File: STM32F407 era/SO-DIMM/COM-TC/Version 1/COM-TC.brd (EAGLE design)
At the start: 127 x 165.1 mm, 126 parts, among them J1 CON1, J2 CON1, J3 SO-DIMM-CPU, J4 FTDI_DEVICE, Q4 PMV20XNE, U1 IRF9332PBF, U10 SN65HVD232D, U11 MAX9926, U12 MCP6004-E/SL, U13 MCP6004-E/SL, U14 MCP6004-E/SL, U17 MC74AC573DWG, U18 MC74AC573DWG, U19 MC74AC573DWG, U2 5V, U20 MC74AC573DWG, U3 TPS54331D, U4 3,3V, U5 MAX9926, U6 MCP6004-E/SL, U7 LoPy, X1 057-014-1

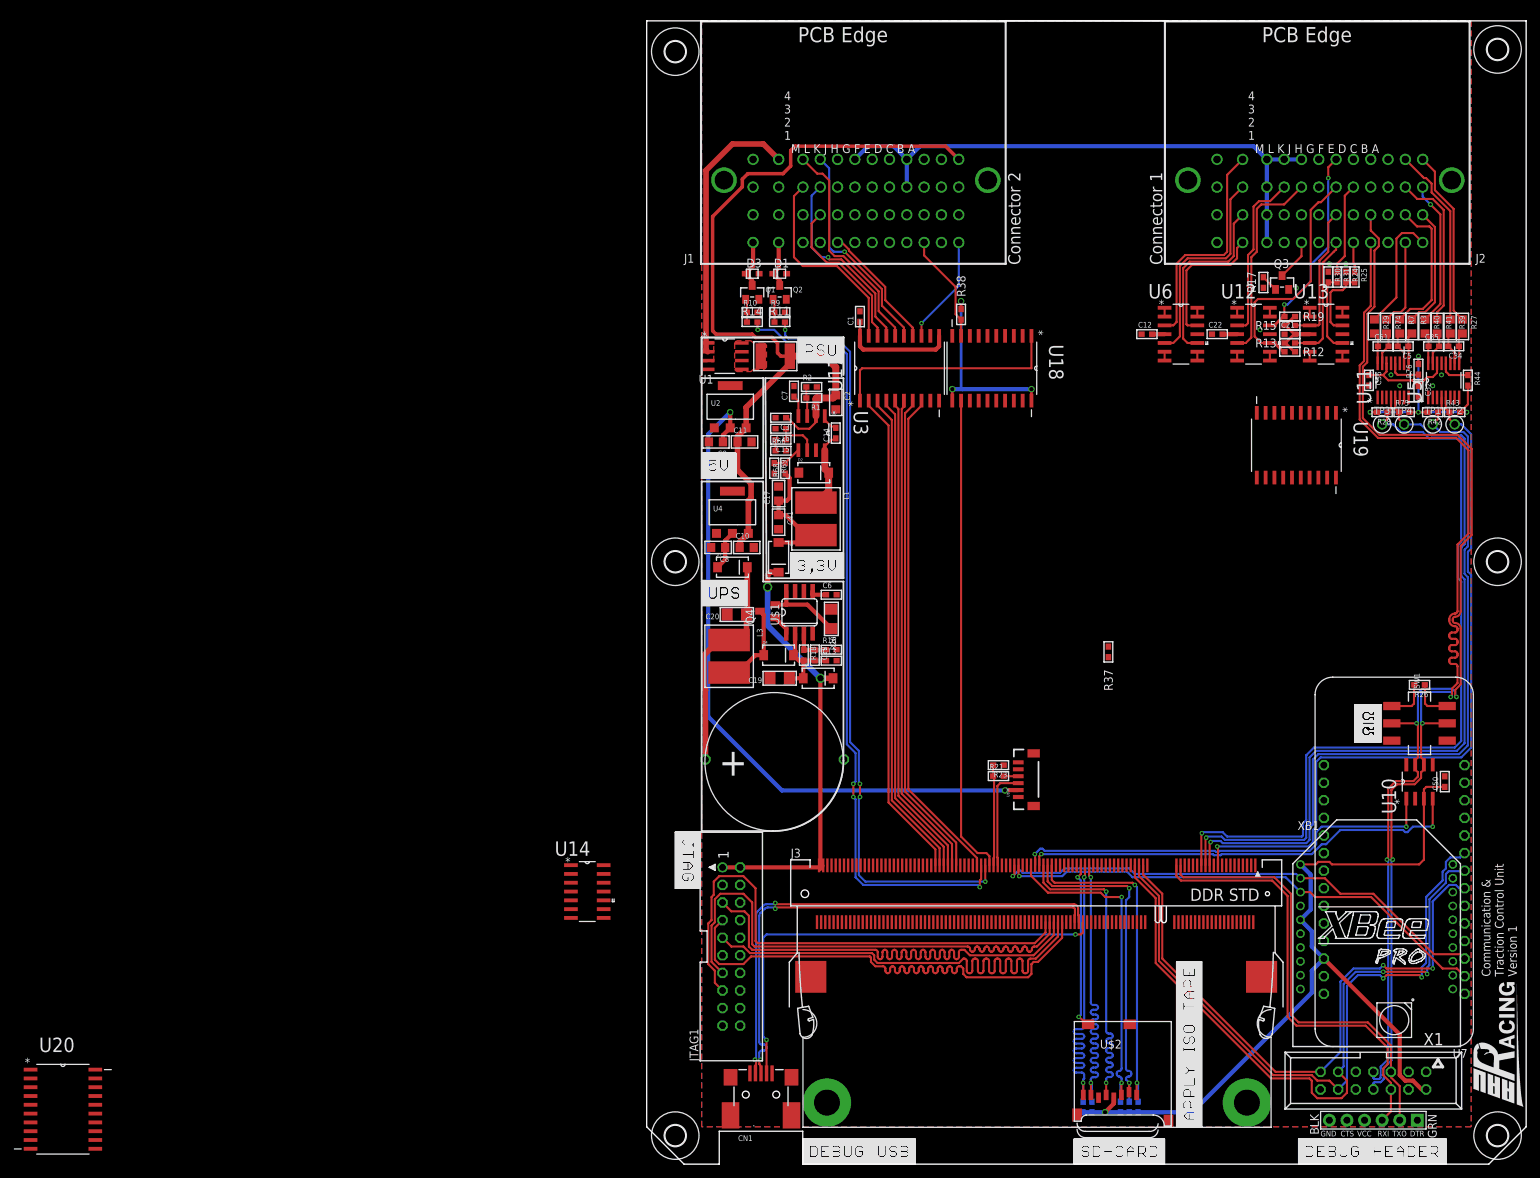
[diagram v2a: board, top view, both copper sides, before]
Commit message: COM/TC RC1 done
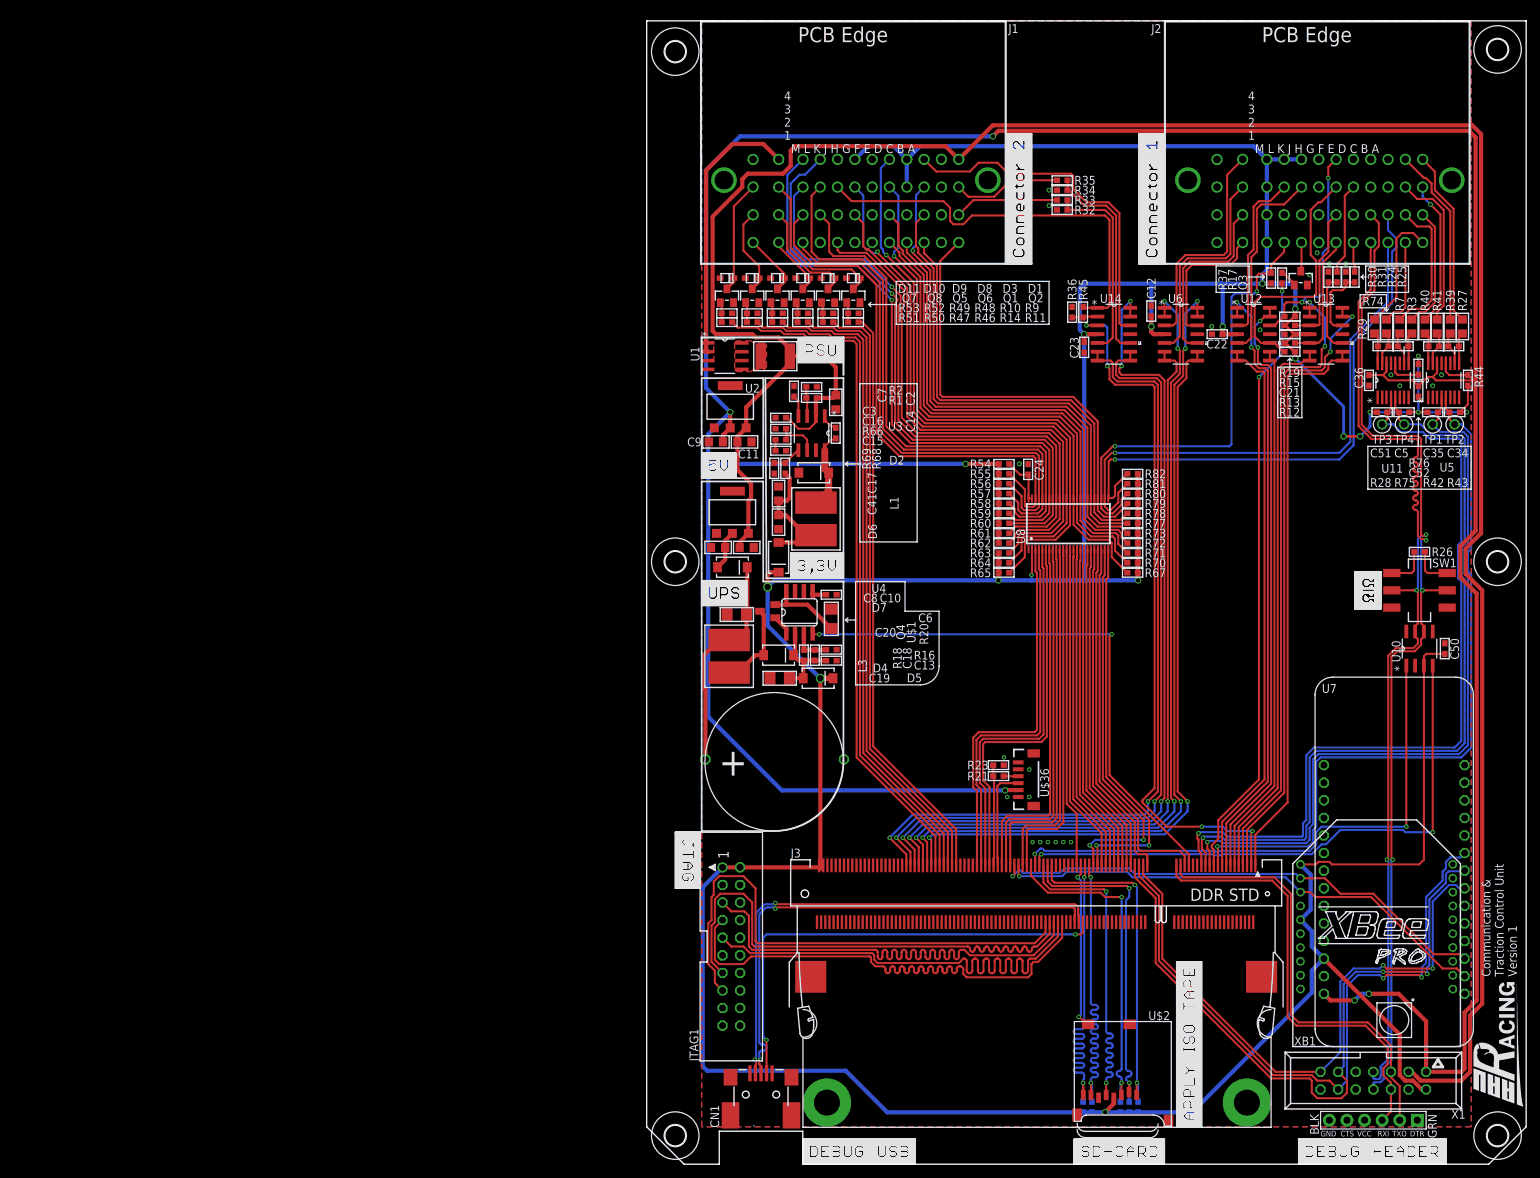
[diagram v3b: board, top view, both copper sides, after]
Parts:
- removed C1: 100n, microbuilder:_0603
- removed R38: 10k, microbuilder:_0603
- removed U17, U18, U19, U20: MC74AC573DWG, ON Semiconductor_By_element14_Batch_1:SOIC127P1030X265-20N
- added C23, C24: 100n, microbuilder:_0603
- added D10, D11, D8, D9: (no value), adafruit:SOD-323F
- added Q5, Q6, Q7, Q8: (no value), microbuilder:SOT23-WIDE
- added R32, R34, R36: 976, microbuilder:_0603
- added R33, R35, R45: 499, microbuilder:_0603
- added R46, R47, R50, R51, R55, R56, R57, R58, R59, R60, R61, R62, R63, R64, R65, R67, R70, R71, R72, R73, R77, R78, R79, R80, R81, R82: 220, microbuilder:_0603
- added R48, R49, R52, R53: 500, microbuilder:_0603
- added R54: 200k, microbuilder:_0603
- added U8: GTL2000, AAU-Racing:TSSOP48
- C10, C11: value (none) -> 10u
- C8, C9: value (none) -> 22u
- moved U14 110.7 mm to (67.5, 119.9)
- moved R37 58.9 mm to (90.2, 128.0)
- moved SW1 19.2 mm to (111.6, 82.9)
- moved C50 19.2 mm to (115.3, 74.5)
- moved U10 19.2 mm to (111.6, 74.5)
- moved R26 19.2 mm to (111.6, 88.4)
- moved D3 11.0 mm to (26.2, 128.0), turned to 0 degrees
- moved Q1 11.0 mm to (26.2, 125.4)
- moved R10 11.0 mm to (26.2, 122.9)
- moved R14 11.0 mm to (26.2, 121.6)
- moved D1 10.7 mm to (29.8, 128.0), turned to 0 degrees
- moved Q2 10.6 mm to (29.8, 125.4)
- moved R9 10.6 mm to (29.8, 122.9)
- moved R11 10.6 mm to (29.8, 121.6)
- moved C12 3.39 mm to (72.9, 123.2), turned to 270 degrees
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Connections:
- removed net BRAKE-POT: J1.C3
- removed net DIG_IO_EN: U17.1, U18.1
- removed net VOUTUB: J3.3
- new net AUX1: J1.G2, R63.2, U8.38
- new net AUX1L: J3.99, U8.11
- new net AUX2: J1.G3, R64.2, U8.37
- new net AUX2L: J3.75, U8.12
- new net AUX3: J1.E4, R65.2, U8.36
- new net AUX3L: J3.63, U8.13
- new net AUX4: J1.E3, R67.2, U8.35
- new net AUX4L: J3.61, U8.14
- new net AUX5: J1.E1, R70.2, U8.34
- new net AUX5L: J3.59, U8.15
- new net AUX6: J1.E2, R71.2, U8.33
- new net AUX6L: J3.57, U8.16
- new net AUX7: J1.D1, R72.2, U8.32
- new net AUX7L: J3.55, U8.17
- new net AUX8: J1.C3, R73.2, U8.31
- new net AUX8L: J3.53, U8.18
- new net AUX9: J1.C2, R77.2, U8.30
- new net AUX9L: J3.51, U8.19
- new net COM_RXB: J3.67, U8.23
- new net COM_TXB: J3.65, U8.24
- new net ECU1L: J3.123, U8.3
- new net ECU2L: J3.121, U8.4
- new net GSENSL: R32.2, R33.2, U14.5
- new net N$13: R36.2, R45.1, U14.2
- new net N$14: Q5.1, R47.1, R49.1
- new net N$20: Q8.1, R50.1, R52.1
- new net N$21: Q7.1, R51.1, R53.1
- new net N$23: C24.1, R54.1, U8.47, U8.48
- new net N$33: J1.H2
- new net N$9: Q6.1, R46.1, R48.1
- new net NEUTRALL: J3.35, U8.22
- new net ODC1: J3.135, R14.2
- new net ODC2: J3.141, R50.2
- new net ODC3: J3.133, R11.2
- new net ODC4: J3.143, R51.2
- new net ODI1: D3.C, J1.L2, Q1.3
- new net ODI2: D10.C, J1.M2, Q8.3
- new net ODI3: D1.C, J1.L3, Q2.3
- new net ODI4: D11.C, J1.M3, Q7.3
- new net VOUTB: J1.H3, R45.2, U14.1
- new net YAWL: R34.2, R35.2, U14.10
- net 3.3V: now also C23.2, R63.1, R64.1, R65.1, R67.1, R70.1, R71.1, R72.1, R73.1, R77.1, R78.1, R79.1, R80.1, R81.1, R82.1, U8.2; no longer R38.1, U18.11, U18.20
- net 5.0V: now also R54.2, R55.1, R56.1, R57.1, R58.1, R59.1, R60.1, R61.1, R62.1; no longer C1.1, U17.11, U17.20
- net BITE: now also R79.2, U8.28; no longer U17.13
- net BITEL: now also J3.41, U8.21; no longer J3.123, U17.8
- net BRAKEPB: now also J3.13; no longer J3.5
- net CLUTCH-POT: now also U14.12
- net CLUTCH-POTB: now also J3.153, U14.13, U14.14; no longer J3.145
- net COM_RX: now also R81.2, U8.26; no longer J3.67
- net COM_TX: now also R82.2, U8.25; no longer J3.65
- net CURRENT1B: now also J3.5; no longer J3.15
- net CURRENT2B: now also J3.1; no longer J3.17
- net ECU1: now also J1.K2, R55.2, U8.46; no longer J2.C4
- net ECU2: now also J1.K1, R56.2, U8.45; no longer J2.D4
- net GEARPOSANB: now also J3.17; no longer J3.9
- net GND: now also C23.1, C24.2, D10.A, D11.A, D8.A, D9.A, Q5.2, Q6.2, Q7.2, Q8.2, R32.1, R34.1, R36.1, R48.2, R49.2, R52.2, R53.2, U14.11, U8.1; no longer C1.2, U17.10, U17.9, U18.10
- net GSENS: now also R33.1
- net GSENSB: now also J3.157, U14.6, U14.7; no longer J3.155
- net HB1-DIRA: now also J3.101, U8.10; no longer J3.133, U17.7
- net HB1-DIRA-IN: now also R62.2, U8.39; no longer U17.14
- net HB1-DIRB: now also J3.109, U8.8; no longer J3.135, U17.6
- net HB1-DIRB-IN: now also R60.2, U8.41; no longer U17.15
- net HB1-PWM: now also J3.119, U8.5; no longer J3.139, U17.4
- net HB1-PWM-IN: now also R57.2, U8.44; no longer U17.17
- net HB2-DIRA: now also J3.107, U8.9; no longer J3.143, U17.2
- net HB2-DIRA-IN: now also R61.2, U8.40; no longer U17.19
- net HB2-DIRB: now also J3.111, U8.7; no longer J3.137, U17.5
- net HB2-DIRB-IN: now also R59.2, U8.42; no longer U17.16
- net HB2-PWM: now also J3.117, U8.6; no longer J3.141, U17.3
- net HB2-PWM-IN: now also R58.2, U8.43; no longer U17.18
- net IGNCUT: now also J3.21
- net NEUTRAL: now also R80.2, U8.27
- net OC1: now also J3.137, R46.2; no longer J3.119, R11.2
- net OC2: now also J3.139, R47.2; no longer J3.121, R14.2
- net OILP: now also R78.2, U8.29; no longer R38.2, U18.9
- net OILPI: now also J3.49, U8.20; no longer J3.117, U18.12
- net RLY1: now also D8.C, Q6.3; no longer D1.C, Q2.3
- net RLY2: now also D9.C, Q5.3; no longer D3.C, Q1.3
- net SPEEDB: now also J3.15; no longer J3.1
- net TRAVEL1B: now also J3.151; no longer J3.147
- net TRAVEL3B: now also J3.145; no longer J3.151
- net TRAVEL4B: now also J3.147; no longer J3.153
- net UPS_EN: now also J3.33
- net VCC: no longer U19.20, U20.20
- net VOUT: now also J3.3, U14.3; no longer J1.H3
- net VTEMP2B: now also J3.11; no longer J3.13
- net VTEMPB: now also J3.9; no longer J3.11
- net YAW: now also R35.1
- net YAWB: now also J3.155, U14.8, U14.9; no longer J3.157
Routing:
- net 5.0V: track 130.9 -> 491.4 mm, vias 2 -> 6
- net 3.3V: track 346.3 -> 628.9 mm, vias 10 -> 18
- net 12V: track 127.9 -> 353.7 mm
- net CLUTCH-POTB: track 0.00 -> 126.2 mm, vias 0 -> 4
- net TRAVEL2B: track 1.27 -> 120.8 mm, vias 0 -> 4
- net TRAVEL4B: track 1.27 -> 120.8 mm, vias 0 -> 4
- net GSENSB: track 0.00 -> 118.7 mm, vias 0 -> 2
- net YAWB: track 0.00 -> 118.2 mm, vias 0 -> 2
- net TRAVEL1B: track 1.27 -> 111.9 mm, vias 0 -> 2
- net TRAVEL3B: track 1.27 -> 111.9 mm, vias 0 -> 2
- net VOUT: track 0.00 -> 102.7 mm, vias 0 -> 4
- net ODC4: track 0.00 -> 99.3 mm
- net ODC2: track 0.00 -> 96.3 mm
- net BRAKEP2B: track 1.27 -> 92.1 mm, vias 0 -> 2
- net CURRENT1B: track 1.27 -> 91.1 mm, vias 0 -> 2
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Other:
- board text removed: "Connector 1"
- board text removed: "Connector 2"

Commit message: All board V1-RC1 done
all boards ready for inspection
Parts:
- removed R63: 220, microbuilder:_0603
- added OK1: 4N33, optocoupler:DIL06
- added R38: 560, microbuilder:_0603
- added R83: 500, microbuilder:_0603
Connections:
- removed net AUX1: J1.G2, R63.2, U8.38
- removed net AUX1L: J3.99, U8.11
- new net CTS: J3.31, U7.23, XB1.12
- new net N$22: OK1.1, R38.2
- new net PWR_OUT: J3.99, OK1.5, R83.2
- new net RTS: J3.29, U7.24, XB1.16
- net 12V: now also R38.1
- net 3.3V: now also R83.1; no longer R63.1
- net GND: now also OK1.2, OK1.4
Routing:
- net AUX1: track 78.3 -> 0.00 mm
- net CTS: track 0.00 -> 56.1 mm, vias 0 -> 2
- net AUX1L: track 50.3 -> 0.00 mm
- net 12V: track 353.7 -> 403.2 mm, vias 0 -> 2
- net RTS: track 0.00 -> 44.9 mm, vias 0 -> 2
- net PWR_OUT: track 0.00 -> 29.7 mm, vias 0 -> 2
- net 3.3V: track 628.9 -> 644.2 mm, vias 18 -> 20
- net N$22: track 0.00 -> 9.88 mm
- net AUX2: track 84.8 -> 84.1 mm
